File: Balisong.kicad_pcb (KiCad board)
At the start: 2 copper layers, 83.4 x 38.1 mm, 24 parts, among them SW1 SW_Push, U1 ATmega32U4-AU, Y1 16MHz

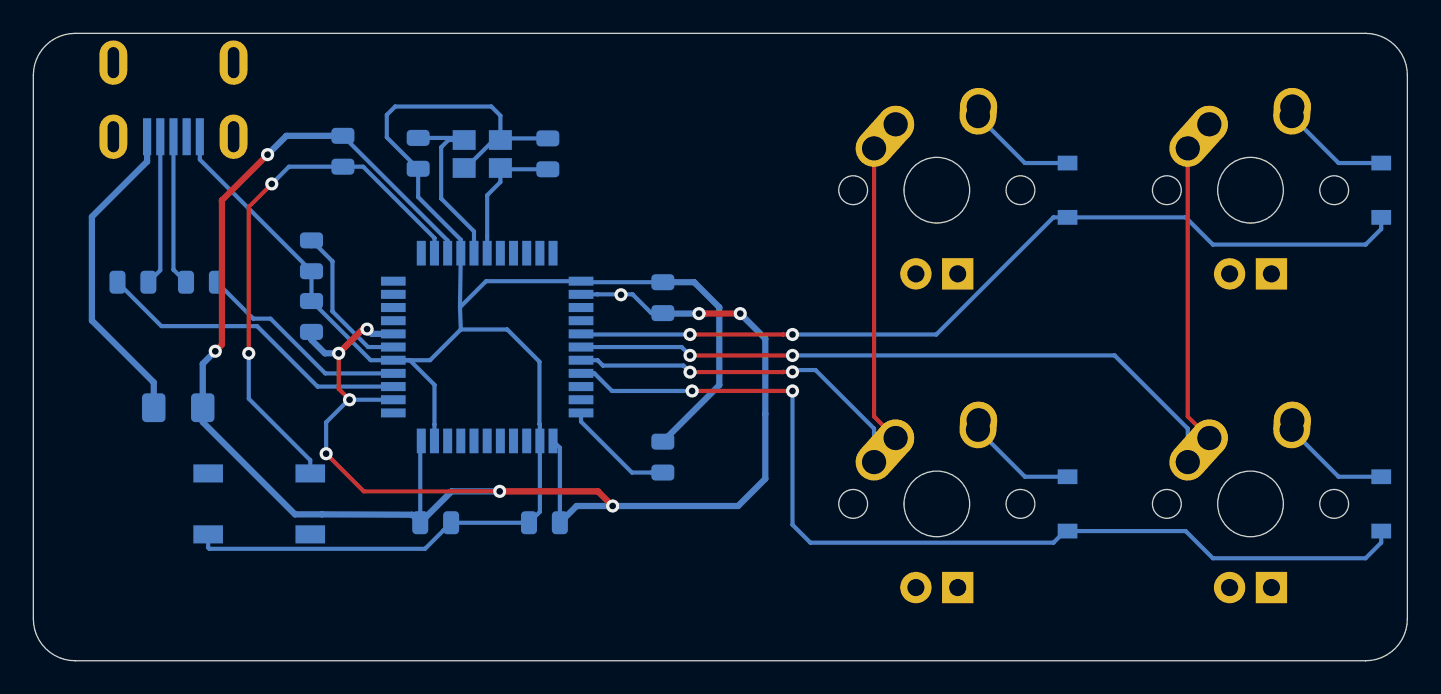
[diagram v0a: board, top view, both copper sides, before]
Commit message: Creating the gerber
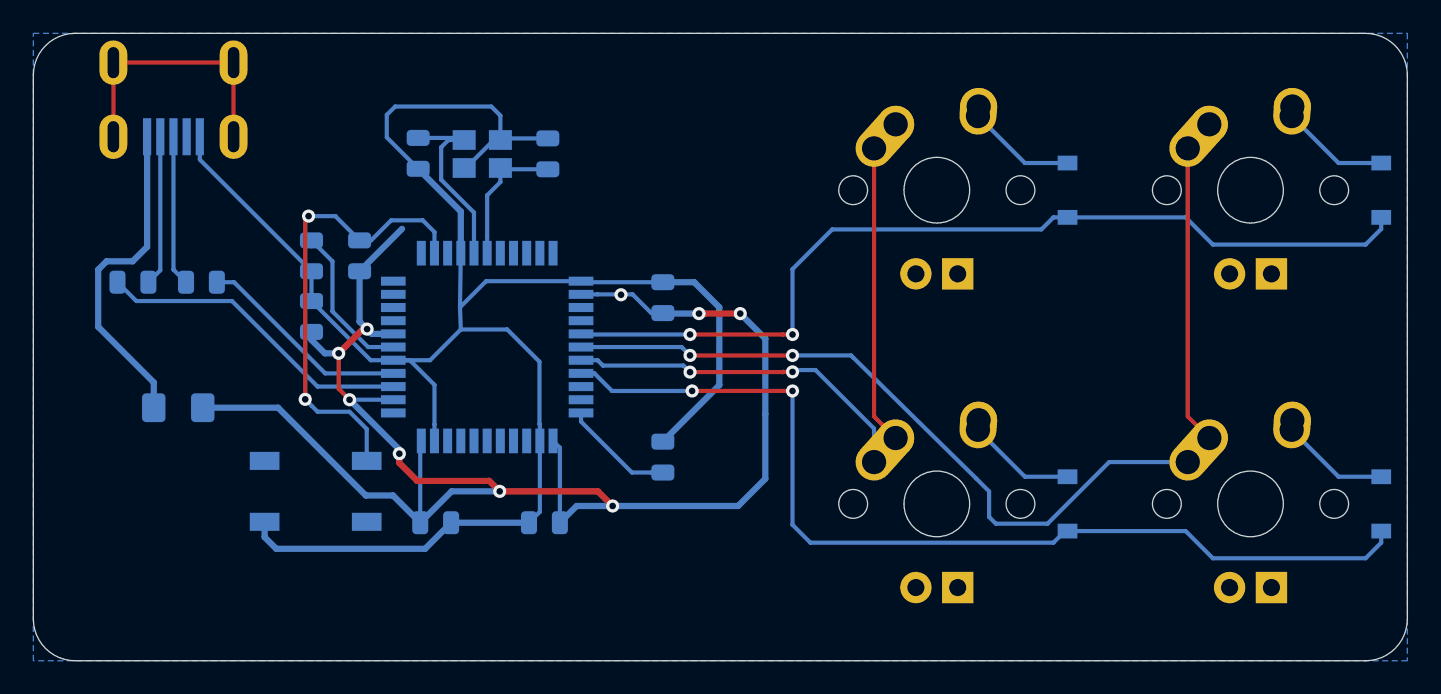
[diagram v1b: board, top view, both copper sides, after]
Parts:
- moved R4 6.43 mm to (47.5, 67.5), turned to 90 degrees
- moved SW1 3.51 mm to (44.8, 81.8)
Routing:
- net +5V: track 133.6 -> 105.1 mm, vias 11 -> 9
- net Net-(USB1-Pad6): track 0.00 -> 16.3 mm
- net Net-(R4-Pad2): track 32.7 -> 28.0 mm
- net GND: track 123.5 -> 120.5 mm
- net COL1: track 59.1 -> 61.8 mm
- net ROW0: track 53.3 -> 55.7 mm
- net VCC: track 19.4 -> 20.0 mm
- added copper zone on B.Cu, net GND
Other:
- board text added: "liwei1997"

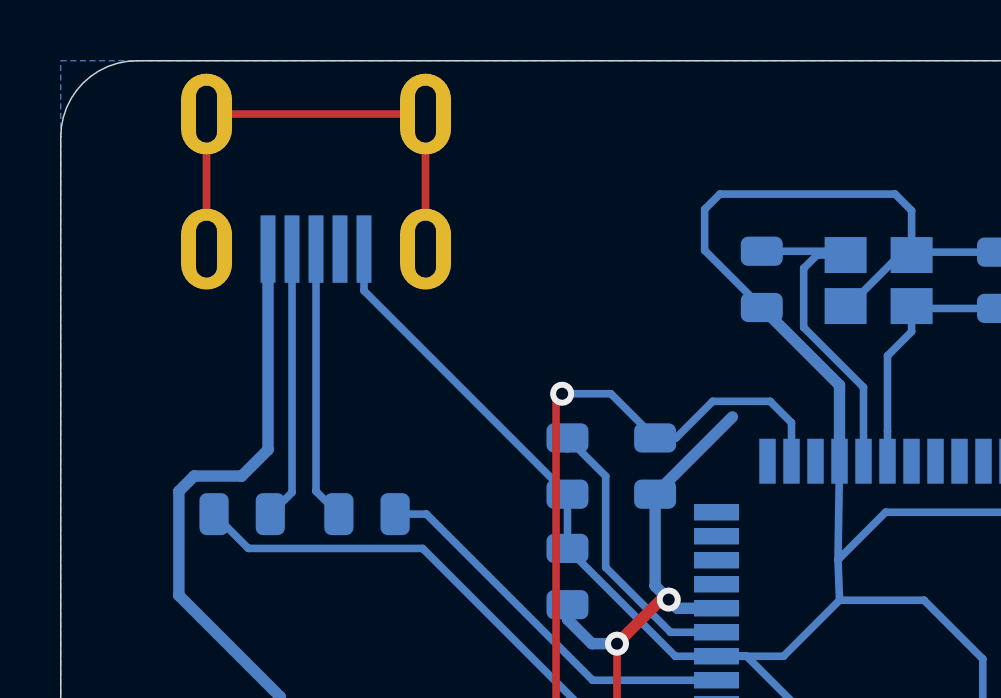
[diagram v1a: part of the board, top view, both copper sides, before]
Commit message: Changed USB connectors
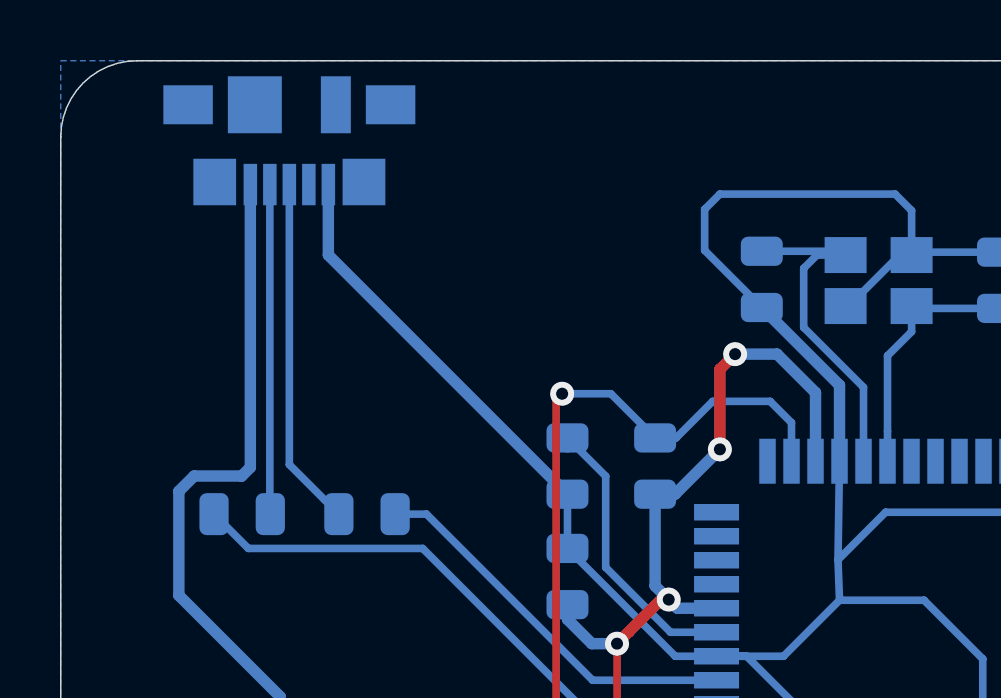
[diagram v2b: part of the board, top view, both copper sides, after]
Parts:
- removed USB1: Molex-0548190589, random-keyboard-parts:Molex-0548190589
- added J1: USB_B_Micro, Connector_USB:USB_Micro-B_Molex_47346-0001, B.Cu at (35.3, 56.6)
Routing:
- net Net-(USB1-Pad6): track 16.3 -> 0.00 mm
- net +5V: track 105.1 -> 113.2 mm, vias 9 -> 11
- net GND: track 120.5 -> 123.1 mm
- net D+: track 9.15 -> 11.7 mm
- net VCC: track 20.0 -> 21.9 mm
- net D-: track 9.88 -> 11.0 mm
